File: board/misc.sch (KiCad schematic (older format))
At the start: 8 parts, among them U17 74AC74, U18 8.0M

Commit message: RC1 of schematic and initial board layout
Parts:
- added C45, C46: 0.1u, Capacitor_THT:C_Rect_L4.6mm_W2.0mm_P2.50mm_MKS02_FKP02, symbol Device:C_Small
- added U16: W65C22SxPL, Package_LCC:PLCC-44_THT-Socket, symbol 65xx:W65C22SxPL
- added U17, U19: CD74AC541E, Package_DIP:DIP-20_W7.62mm_Socket, symbol 74xx:74LS541
- added U21: SN74AHCT245N, Package_DIP:DIP-20_W7.62mm_Socket, symbol 74xx:74HC245
- C41: renamed from C26; footprint (none) -> Capacitor_THT:CP_Radial_D5.0mm_P2.00mm
- C42: renamed from C27; footprint (none) -> Capacitor_THT:CP_Radial_D5.0mm_P2.00mm
- C43: renamed from C28; footprint (none) -> Capacitor_THT:CP_Radial_D5.0mm_P2.00mm
- C44: renamed from C29; footprint (none) -> Capacitor_THT:CP_Radial_D5.0mm_P2.00mm
- R1, R2: footprint (none) -> Resistor_THT:R_Axial_DIN0207_L6.3mm_D2.5mm_P10.16mm_Horizontal
- U18: renamed from U17; value 74AC74 -> SN74AC74N; footprint (none) -> Package_DIP:DIP-14_W7.62mm_Socket
- U20: renamed from U18; footprint (none) -> Package_DIP:DIP-8_W7.62mm_Socket
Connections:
- net +5V: now also C45.1, C46.1, U16.21 (VDD), U16.26 (CS1), U17.20 (VCC), U19.20 (VCC), U21.20 (VCC)
- net GND: now also C45.2, C46.2, U16.1 (VSS), U17.1 (G1), U17.10 (GND), U17.19 (G2), U17.6 (A4), U17.7 (A5), U17.8 (A6), U17.9 (A7), U19.1 (G1), U19.10 (GND), U19.19 (G2), U21.10 (GND)
- net PHI2: now also U16.27 (ϕ2), U17.2 (A0)
- new net A0: U16.42 (RS0), U19.2 (A0)
- new net A1: U16.41 (RS1), U19.3 (A1)
- new net A2: U16.40 (RS2), U19.4 (A2)
- new net A3: U16.39 (RS3), U19.5 (A3)
- new net A4: U19.6 (A4)
- new net A5: U19.7 (A5)
- new net A6: U19.8 (A6)
- new net A7: U19.9 (A7)
- new net CA1: U16.44 (CA1)
- new net CA2: U16.43 (CA2)
- new net CB1: U16.19 (CB1)
- new net CB2: U16.20 (CB2)
- new net D0: U16.36 (D0), U21.18 (B0)
- new net D1: U16.35 (D1), U21.17 (B1)
- new net D2: U16.34 (D2), U21.16 (B2)
- new net D3: U16.32 (D3), U21.15 (B3)
- new net D4: U16.31 (D4), U21.14 (B4)
- new net D5: U16.30 (D5), U21.13 (B5)
- new net D6: U16.29 (D6), U21.12 (B6)
- new net D7: U16.28 (D7), U21.11 (B7)
- new net PA0: U16.2 (PA0)
- new net PA1: U16.3 (PA1)
- new net PA2: U16.4 (PA2)
- new net PA3: U16.5 (PA3)
- new net PA4: U16.6 (PA4)
- new net PA5: U16.7 (PA5)
- new net PA6: U16.8 (PA6)
- new net PA7: U16.9 (PA7)
- new net PB0: U16.10 (PB0)
- new net PB1: U16.12 (PB1)
- new net PB2: U16.13 (PB2)
- new net PB3: U16.14 (PB3)
- new net PB4: U16.15 (PB4)
- new net PB5: U16.16 (PB5)
- new net PB6: U16.17 (PB6)
- new net PB7: U16.18 (PB7)
- new net RDB: U17.4 (A2)
- new net RESETB: U16.37 (~RES)
- new net RWB: U16.24 (R/~W), U17.3 (A1), U21.1 (A->B)
- new net SLOTENB: U21.19 (CE)
- new net VIAIRQB: U16.23 (~IRQ)
- new net VIASELB: U16.25 (~CS2)
- new net WRB: U17.5 (A3)
- new net XA0: U19.18 (Y0)
- new net XA1: U19.17 (Y1)
- new net XA2: U19.16 (Y2)
- new net XA3: U19.15 (Y3)
- new net XA4: U19.14 (Y4)
- new net XA5: U19.13 (Y5)
- new net XA6: U19.12 (Y6)
- new net XA7: U19.11 (Y7)
- new net XD0: U21.2 (A0)
- new net XD1: U21.3 (A1)
- new net XD2: U21.4 (A2)
- new net XD3: U21.5 (A3)
- new net XD4: U21.6 (A4)
- new net XD5: U21.7 (A5)
- new net XD6: U21.8 (A6)
- new net XD7: U21.9 (A7)
- new net XPHI2: U17.18 (Y0)
- new net XRDB: U17.16 (Y2)
- new net XRWB: U17.17 (Y1)
- new net XWRB: U17.15 (Y3)
- no-connect marks 4 -> 8
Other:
- note removed: "Bypass Capacitors"
- moved on the sheet: R1, R2, U18A, U18B, U18C, U20

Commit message: RC1 of schematic and initial board layout
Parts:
- removed C44: 1u, Capacitor_THT:CP_Radial_D5.0mm_P2.00mm, symbol Device:C_Small
- removed C45, C46: 0.1u, Capacitor_THT:C_Rect_L4.6mm_W2.0mm_P2.50mm_MKS02_FKP02, symbol Device:C_Small
- removed U17, U19: CD74AC541E, Package_DIP:DIP-20_W7.62mm_Socket, symbol 74xx:74LS541
- removed U21: SN74AHCT245N, Package_DIP:DIP-20_W7.62mm_Socket, symbol 74xx:74HC245
- C35: renamed from C41; value 1u -> 0.1u; footprint Capacitor_THT:CP_Radial_D5.0mm_P2.00mm -> Capacitor_THT:C_Rect_L4.6mm_W2.0mm_P2.50mm_MKS02_FKP02
- C36: renamed from C42; value 1u -> 0.1u; footprint Capacitor_THT:CP_Radial_D5.0mm_P2.00mm -> Capacitor_THT:C_Rect_L4.6mm_W2.0mm_P2.50mm_MKS02_FKP02
- C37: renamed from C43; value 1u -> 0.1u; footprint Capacitor_THT:CP_Radial_D5.0mm_P2.00mm -> Capacitor_THT:C_Rect_L4.6mm_W2.0mm_P2.50mm_MKS02_FKP02
- renumbered U18 to U17, U20 to U18
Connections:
- no-connect marks 8 -> 2
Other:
- moved on the sheet: R1, R2, U16, U17A, U17B, U17C, U18

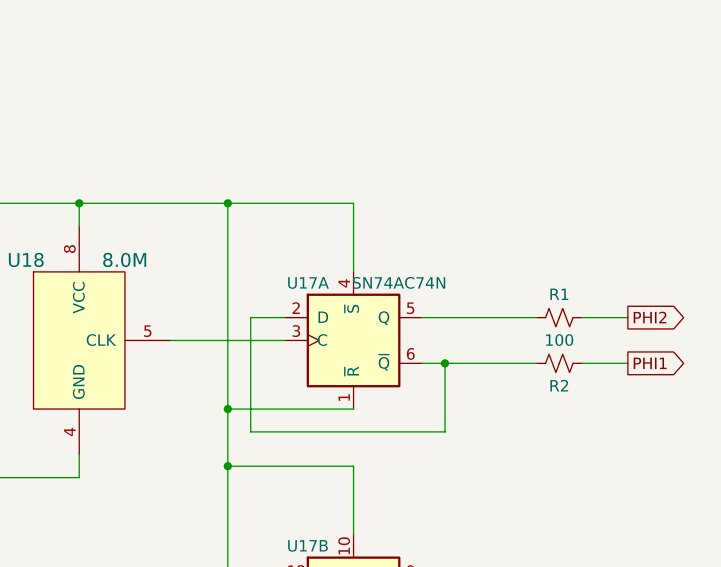
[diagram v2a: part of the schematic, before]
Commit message: Fix footprint for RESET and NMI button handlers Fix symbol for '573 latch
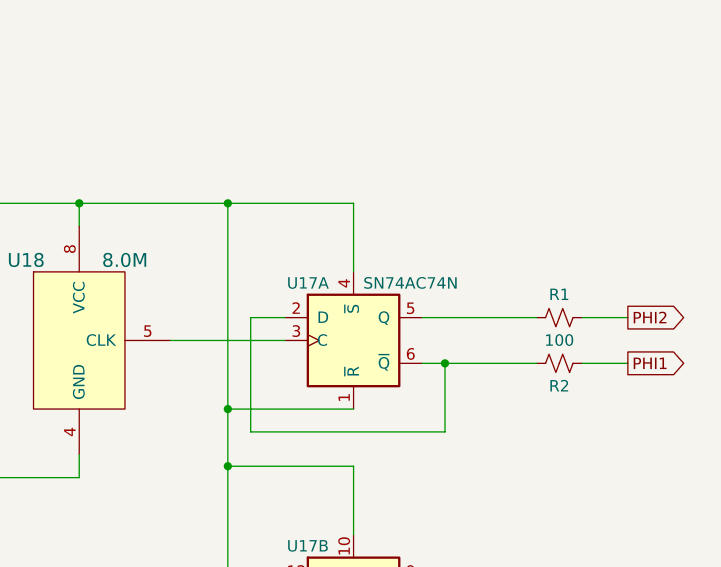
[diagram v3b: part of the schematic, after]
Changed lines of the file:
@@
 P 7800 3450
 F 0 "U17" H 7600 3700 50  0000 C CNN
-F 1 "SN74AC74N" H 8000 3700 50  0000 C CNN
+F 1 "SN74AC74N" H 8050 3700 50  0000 C CNN
 F 2 "Package_DIP:DIP-14_W7.62mm_Socket" H 7800 3450 50  0001 C CNN
 F 3 "" H 7800 3450 50  0001 C CNN
